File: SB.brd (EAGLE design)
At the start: 68 x 30 mm, 30 parts, among them IC1 ATMEGA32U4NT-TQFP, J1 USB-6P-SMT, J3 AUDIO-JACK-PJ321, J4 NO/NC, J5 RJ10-WURTH, K1 HE721C-DIP, Q1 2N7002

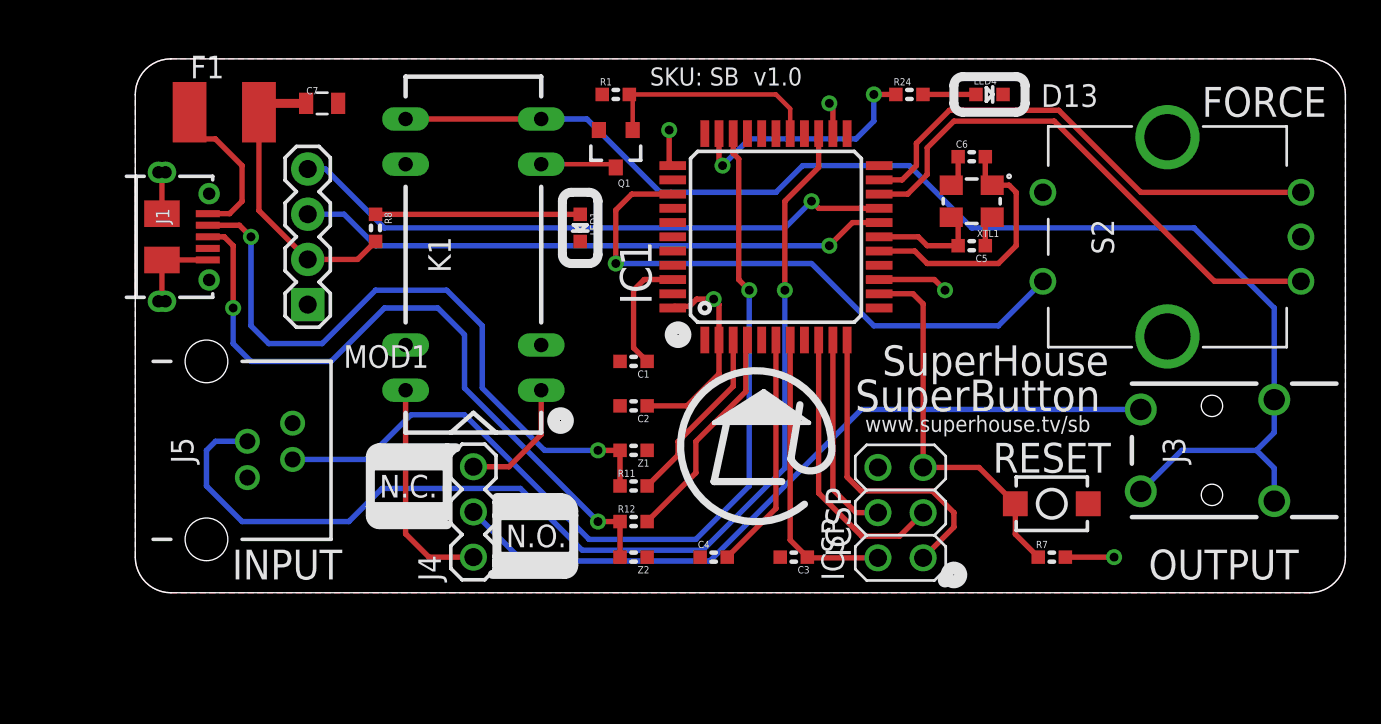
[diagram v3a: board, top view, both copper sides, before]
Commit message: Replaced RJ10 socket with RJ12 and added haptic feedback output
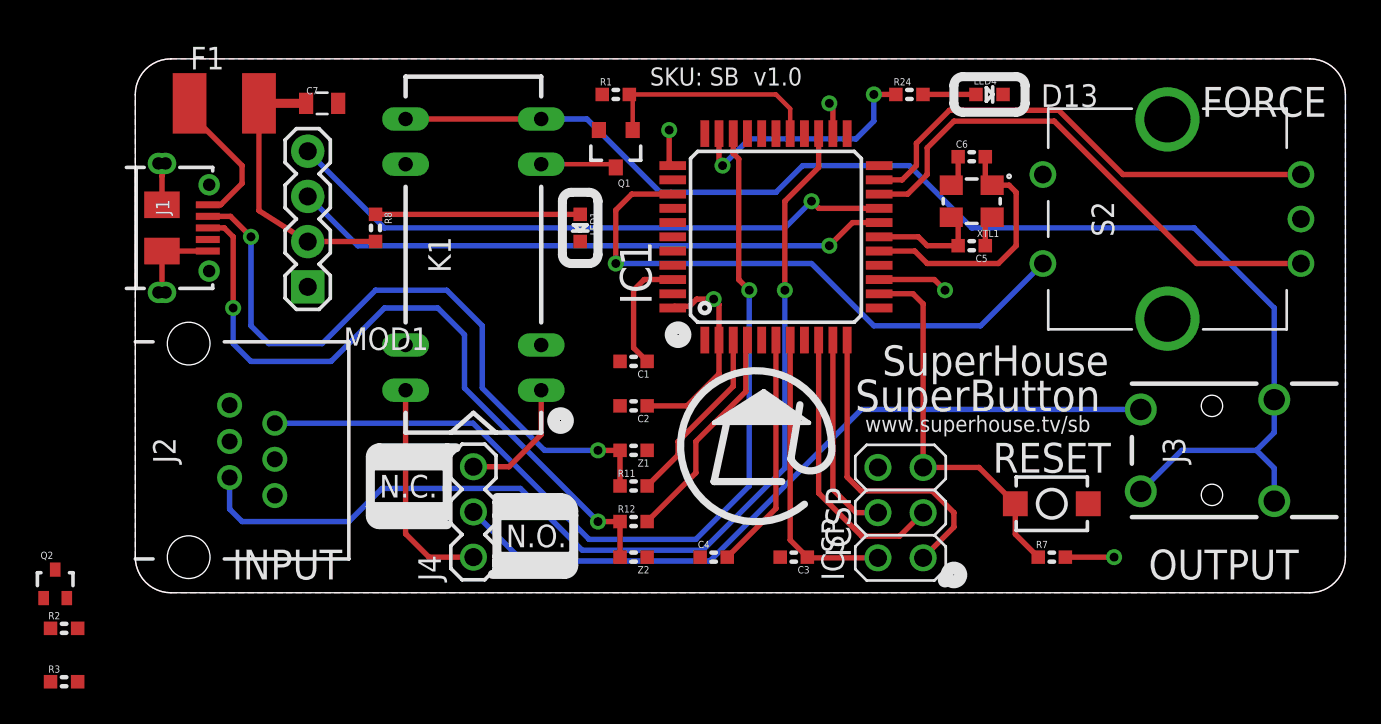
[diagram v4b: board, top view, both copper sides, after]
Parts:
- removed J5: RJ10-WURTH, SuperHouse-Connectors:RJ10
- added J2: RJ12, SuperHouse-Connectors:RJ12
- added Q2: RJU003N03, SuperHouse-DiscreteSemi:SOT32-3
- added R2: 150R, SuperHouse-DiscreteSemi:R0603
- added R3: 10K, SuperHouse-DiscreteSemi:R0603
- moved MOD1 1.00 mm to (28.0, 22.0)
- moved S2 1.00 mm to (58.0, 22.0)
- moved F1 0.50 mm to (5.00, 28.5)
- moved J1 0.50 mm to (1.50, 21.5)
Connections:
- new net N$2: J2.6, R2.2
- new net N$8: Q2.3, R2.1
- net 5V: now also J2.3, J2.4; no longer J5.P$1
- net D12: now also Q2.1, R3.2
- net D4_A6: now also J2.5; no longer J5.P$3
- net D5: now also J2.2; no longer J5.P$2
- net GND: now also J2.1, Q2.2, R3.1; no longer J5.P$4
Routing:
- net D4_A6: track 61.5 -> 57.0 mm
- net 5V: track 56.2 -> 55.2 mm
- net USB+: track 9.36 -> 8.70 mm
- net GND: track 10.9 -> 11.4 mm
- net D+: track 39.3 -> 39.8 mm

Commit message: Routing for haptic feedback
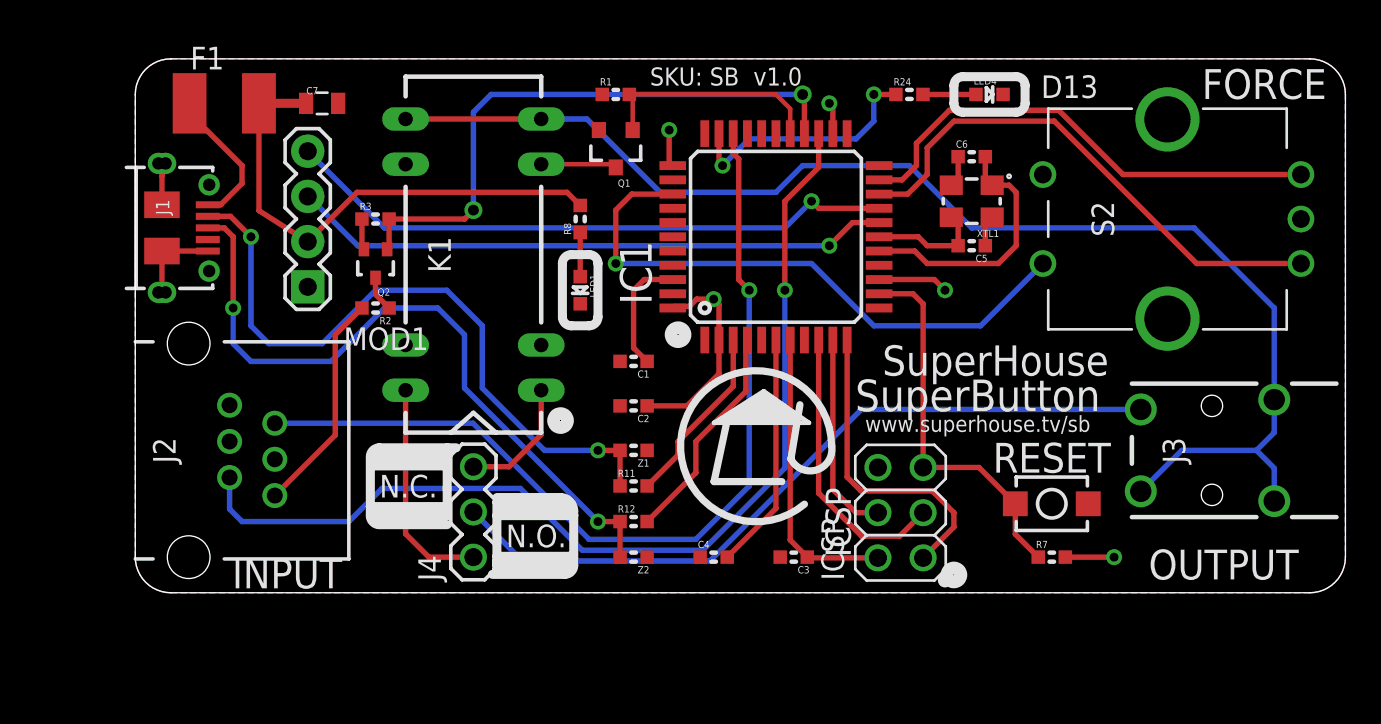
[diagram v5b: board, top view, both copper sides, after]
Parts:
- moved R3 31.3 mm to (13.5, 22.0)
- moved Q2 25.5 mm to (13.5, 19.5), turned to 180 degrees
- moved R2 25.1 mm to (13.5, 17.0), turned to 180 degrees
- moved R8 11.5 mm to (25.0, 22.0), turned to 90 degrees
- moved LED1 3.50 mm to (25.0, 18.0)
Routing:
- net D12: track 0.00 -> 33.3 mm, vias 0 -> 2
- net 5V: track 55.2 -> 68.1 mm
- net N$2: track 0.00 -> 12.6 mm
- net N$5: track 11.5 -> 2.48 mm
- net N$8: track 0.00 -> 2.02 mm
- net GND: track 11.4 -> 13.2 mm

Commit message: ERC / DRC for v1.0 release
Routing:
- net USB+: track 8.70 -> 8.14 mm
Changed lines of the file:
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@@
 <?xml version="1.0" encoding="utf-8"?>
 <!DOCTYPE eagle SYSTEM "eagle.dtd">
-<eagle version="9.5.2">
+<eagle version="9.5.1">
 <drawing>
 <settings>
@@
 <signal name="A0">
 <contactref element="IC1" pad="36"/>
-<wire x1="30.2" y1="23.4" x2="30.1072" y2="23.4928" width="0.3048" layer="1"/>
 <wire x1="30.2" y1="23.4" x2="27.9" y2="23.4" width="0.3048" layer="1"/>
 <wire x1="27.9" y1="23.4" x2="27" y2="22.5" width="0.3048" layer="1"/>
@@
 <contactref element="F1" pad="1"/>
 <wire x1="6" y1="24" x2="6" y2="25" width="0.3048" layer="1"/>
-<wire x1="3" y1="27.95" x2="3.05" y2="28.5" width="0.3048" layer="1"/>
 <wire x1="4.075" y1="22.8" x2="4.8" y2="22.8" width="0.3048" layer="1"/>
 <wire x1="4.8" y1="22.8" x2="6" y2="24" width="0.3048" layer="1"/>
@@
 <wire x1="14.262" y1="22" x2="18.5" y2="22" width="0.3048" layer="1"/>
 <wire x1="18.5" y1="22" x2="19" y2="22.5" width="0.3048" layer="1"/>
-<via x="19" y="22.5" extent="1-16" drill="0.6096"/>
+<via x="19" y="22.5" extent="1-16" drill="0.5"/>
 <wire x1="19" y1="22.5" x2="19" y2="28" width="0.3048" layer="16"/>
 <wire x1="20" y1="29" x2="37.5" y2="29" width="0.3048" layer="16"/>
-<via x="37.5" y="29" extent="1-16" drill="0.6096"/>
+<via x="37.5" y="29" extent="1-16" drill="0.5"/>
 <wire x1="37.5" y1="29" x2="37.6" y2="28.9" width="0.3048" layer="1"/>
 <wire x1="37.6" y1="28.9" x2="37.6" y2="26.8" width="0.3048" layer="1"/>

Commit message: Tweaks and cleanup, hopefully for v1.1 release
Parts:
- added R4: 10K, SuperHouse-DiscreteSemi:R0603
- Q2: value RJU003N03 -> 2N7002; device SuperHouse-DiscreteSemi:SOT32-3 -> SuperHouse-DiscreteSemi:SOT23-3
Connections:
- net 5V: now also R4.2
- net A0: now also R4.1
- net N$7: no longer J3.2
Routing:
- net N$7: track 73.6 -> 65.3 mm
- net 5V: track 68.1 -> 71.3 mm
- net A0: track 33.5 -> 36.5 mm
- net D2_SDA: track 34.7 -> 35.7 mm
- net D3_SCL: track 33.8 -> 34.6 mm
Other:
- board text added: "SKU: SB v1.1"
- board text removed: "SKU: SB v1.0"
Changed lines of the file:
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@@
 <?xml version="1.0" encoding="utf-8"?>
 <!DOCTYPE eagle SYSTEM "eagle.dtd">
-<eagle version="9.5.1">
+<eagle version="9.5.2">
 <drawing>
 <settings>
@@
 <setting verticaltext="up"/>
 </settings>
-<grid distance="0.5" unitdist="mm" unit="mm" style="lines" multiple="1" display="yes" altdistance="0.005" altunitdist="inch" altunit="inch"/>
+<grid distance="1" unitdist="mm" unit="mm" style="lines" multiple="1" display="yes" altdistance="0.005" altunitdist="inch" altunit="inch"/>
 <layers>
 <layer number="1" name="Top" color="12" fill="1" visible="yes" active="yes"/>
@@
 </layers>
 <board>
-<fusionsync huburn="a.cGVyc29uYWw6dWUyZDliZmNi" projecturn="a.cGVyc29uYWw6dWUyYmY2YTMwIzIwMTkxMjAzMjQ0MDMwNjUx" f3durn="urn:adsk.wipprod:dm.lineage:0njJKfu6R3STVv2jK1C-rg" pcbguid="d3339778-c5ae-47ed-addf-8a81f3fd190a" lastpulledtime="" lastsyncedchangeguid="e466276c-e581-ef05-ad4f-067f72518912"/>
+<fusionsync huburn="a.cGVyc29uYWw6dWUyZDliZmNi" projecturn="a.cGVyc29uYWw6dWUyYmY2YTMwIzIwMTkxMjAzMjQ0MDMwNjUx" f3durn="urn:adsk.wipprod:dm.lineage:0njJKfu6R3STVv2jK1C-rg" pcbguid="d3339778-c5ae-47ed-addf-8a81f3fd190a" lastpulledtime="" lastsyncedchangeguid="2cfb86e1-d0d8-e218-d1b3-489442767fc3"/>
 <plain>
 <wire x1="66" y1="31" x2="2" y2="31" width="0" layer="20"/>
@@
 <wire x1="68" y1="29" x2="66" y2="31" width="0" layer="20" curve="90"/>
 <text x="51.5" y="7.746" size="1.6764" layer="21" font="vector" ratio="15" align="bottom-center">RESET</text>
-<text x="28.92" y="29.5" size="1.016" layer="21" font="vector" ratio="18">SKU: SB  v1.0</text>
+<text x="28.92" y="29.5" size="1.016" layer="21" font="vector" ratio="18">SKU: SB  v1.1</text>
 <wire x1="39.126" y1="9.278" x2="37.602" y2="5.976" width="0.4064" layer="21" curve="309.2564"/>
 <wire x1="39.126" y1="9.278" x2="36.84" y2="8.516" width="0.4064" layer="21" curve="-163.361194"/>
@@
 <text x="47.34" y="10.04" size="0.9" layer="21" font="vector" ratio="18" align="bottom-center">www.superhouse.tv/sb</text>
 <text x="48.34" y="13.2" size="1.7" layer="21" font="vector" ratio="18" align="bottom-center">SuperHouse</text>
+<wire x1="20.75" y1="5.75" x2="24" y2="5.75" width="1.016" layer="21"/>
+<wire x1="20.75" y1="2.5" x2="24" y2="2.5" width="1.016" layer="21"/>
+<wire x1="17" y1="5.25" x2="14" y2="5.25" width="1.016" layer="21"/>
+<wire x1="13.75" y1="8.5" x2="17" y2="8.5" width="1.016" layer="21"/>
 </plain>
 <attributes>
@@
 <attribute name="VALUE" x="-1" y="9" size="1.27" layer="27" rot="R270" align="bottom-center"/>
 </element>
-<element name="Q2" library="SuperHouse-DiscreteSemi" library_urn="urn:adsk.eagle:library:11768461" package="SOT32-3" package3d_urn="urn:adsk.eagle:package:7066313/2" value="RJU003N03" x="13.5" y="19.5" smashed="yes" rot="R180">
+<element name="Q2" library="SuperHouse-DiscreteSemi" library_urn="urn:adsk.eagle:library:11768461" package="SOT23-3" package3d_urn="urn:adsk.eagle:package:11815952/3" value="2N7002" x="13.5" y="19.5" smashed="yes" rot="R180">
 <attribute name="NAME" x="14.3255" y="18.1" size="0.4064" layer="25" rot="R180"/>
 <attribute name="VALUE" x="14.3" y="19.6905" size="0.3048" layer="27" rot="R180"/>
@@
 <attribute name="NAME" x="12.611" y="22.508" size="0.4064" layer="25" font="vector"/>
 <attribute name="VALUE" x="12.484" y="21.0348" size="0.4064" layer="27" font="vector"/>
+</element>
+<element name="R4" library="SuperHouse-DiscreteSemi" library_urn="urn:adsk.eagle:library:11768461" package="R0603" package3d_urn="urn:adsk.eagle:package:11768543/2" value="10K" x="49" y="17" smashed="yes" rot="R180">
+<attribute name="NAME" x="49.889" y="16.492" size="0.4064" layer="25" font="vector" rot="R180"/>
+<attribute name="VALUE" x="50.016" y="17.9652" size="0.4064" layer="27" font="vector" rot="R180"/>
 </element>
 </elements>
@@
 <wire x1="38" y1="19.5" x2="41.5" y2="16" width="0.3048" layer="16"/>
 <wire x1="41.5" y1="16" x2="47.5" y2="16" width="0.3048" layer="16"/>
+<contactref element="R4" pad="1"/>
+<wire x1="49.762" y1="17" x2="51" y2="18.238" width="0.3048" layer="1"/>
+<wire x1="51" y1="18.238" x2="51" y2="19.5" width="0.3048" layer="1"/>
 </signal>
 <signal name="A1">
@@
 <wire x1="9.69" y1="20.73" x2="12.46" y2="23.5" width="0.3048" layer="1"/>
 <wire x1="12.46" y1="23.5" x2="24.262" y2="23.5" width="0.3048" layer="1"/>
+<contactref element="R4" pad="2"/>
+<wire x1="48.238" y1="17" x2="47.238" y2="18" width="0.3048" layer="1"/>
+<wire x1="47.238" y1="18" x2="45.5" y2="18" width="0.3048" layer="1"/>
 </signal>
 <signal name="RESET">
@@
 <contactref element="R3" pad="1"/>
 <wire x1="12.738" y1="22" x2="12.738" y2="20.412" width="0.3048" layer="1"/>
-<wire x1="12.738" y1="20.412" x2="12.85" y2="20.3" width="0.3048" layer="1"/>
+<wire x1="12.738" y1="20.412" x2="12.55" y2="20.5" width="0.3048" layer="1"/>
 </signal>
 <signal name="3V3">
@@
 <contactref element="R3" pad="2"/>
 <wire x1="14.262" y1="22" x2="14.262" y2="20.412" width="0.3048" layer="1"/>
-<wire x1="14.262" y1="20.412" x2="14.15" y2="20.3" width="0.3048" layer="1"/>
-<wire x1="14.262" y1="22" x2="18.5" y2="22" width="0.3048" layer="1"/>
-<wire x1="18.5" y1="22" x2="19" y2="22.5" width="0.3048" layer="1"/>
-<via x="19" y="22.5" extent="1-16" drill="0.5"/>
-<wire x1="19" y1="22.5" x2="19" y2="28" width="0.3048" layer="16"/>
+<wire x1="14.262" y1="20.412" x2="14.45" y2="20.5" width="0.3048" layer="1"/>
+<wire x1="14.262" y1="22" x2="19" y2="22" width="0.3048" layer="1"/>
+<via x="19" y="22" extent="1-16" drill="0.5"/>
+<wire x1="19" y1="22" x2="19" y2="28" width="0.3048" layer="16"/>
 <wire x1="20" y1="29" x2="37.5" y2="29" width="0.3048" layer="16"/>
 <via x="37.5" y="29" extent="1-16" drill="0.5"/>
@@
 <signal name="D4_A6">
 <contactref element="IC1" pad="25"/>
-<wire x1="38.4" y1="26.8" x2="38.4" y2="24.9" width="0.3048" layer="1"/>
-<wire x1="36.5" y1="23" x2="36.5" y2="18" width="0.3048" layer="1"/>
+<wire x1="38.4" y1="26.8" x2="38.4" y2="25.65" width="0.3048" layer="1"/>
+<wire x1="36.5" y1="23.75" x2="36.5" y2="18" width="0.3048" layer="1"/>
 <via x="36.5" y="18" extent="1-16" drill="0.5"/>
-<wire x1="38.4" y1="24.9" x2="36.5" y2="23" width="0.3048" layer="1"/>
+<wire x1="38.4" y1="25.65" x2="36.5" y2="23.75" width="0.3048" layer="1"/>
 <wire x1="36.5" y1="18" x2="36.5" y2="8" width="0.3048" layer="16"/>
 <wire x1="31.8904" y1="3.3904" x2="25.1096" y2="3.3904" width="0.3048" layer="16"/>
@@
 <contactref element="IC1" pad="19"/>
 <contactref element="MOD1" pad="SDA"/>
-<wire x1="36.5" y1="21.5" x2="14" y2="21.5" width="0.3048" layer="16"/>
-<wire x1="36.5" y1="21.5" x2="38" y2="23" width="0.3048" layer="16"/>
-<via x="38" y="23" extent="1-16" drill="0.5"/>
-<wire x1="38" y1="23" x2="38.4" y2="22.6" width="0.3048" layer="1"/>
-<wire x1="38.4" y1="22.6" x2="41.8" y2="22.6" width="0.3048" layer="1"/>
-<wire x1="14" y1="21.5" x2="9.69" y2="25.81" width="0.3048" layer="16"/>
+<wire x1="37" y1="21.5" x2="22.5" y2="21.5" width="0.3048" layer="16"/>
+<wire x1="22.5" y1="21.5" x2="21.25" y2="20.25" width="0.3048" layer="16"/>
+<wire x1="21.25" y1="20.25" x2="15.25" y2="20.25" width="0.3048" layer="16"/>
+<wire x1="37" y1="21.5" x2="38.5" y2="23" width="0.3048" layer="16"/>
+<via x="38.5" y="23" extent="1-16" drill="0.5"/>
+<wire x1="38.9" y1="22.6" x2="38.5" y2="23" width="0.3048" layer="1"/>
+<wire x1="38.9" y1="22.6" x2="41.8" y2="22.6" width="0.3048" layer="1"/>
+<wire x1="15.25" y1="20.25" x2="9.69" y2="25.81" width="0.3048" layer="16"/>
 </signal>
 <signal name="D3_SCL">
 <contactref element="IC1" pad="18"/>
 <contactref element="MOD1" pad="SCL"/>
-<wire x1="12.5" y1="20.5" x2="39" y2="20.5" width="0.3048" layer="16"/>
+<wire x1="13.5" y1="19.5" x2="21.5" y2="19.5" width="0.3048" layer="16"/>
+<wire x1="21.5" y1="19.5" x2="22.5" y2="20.5" width="0.3048" layer="16"/>
+<wire x1="22.5" y1="20.5" x2="39" y2="20.5" width="0.3048" layer="16"/>
 <via x="39" y="20.5" extent="1-16" drill="0.5"/>
 <wire x1="39" y1="20.5" x2="40.3" y2="21.8" width="0.3048" layer="1"/>
 <wire x1="40.3" y1="21.8" x2="41.8" y2="21.8" width="0.3048" layer="1"/>
 <wire x1="9.73" y1="23.27" x2="9.69" y2="23.27" width="0.3048" layer="16"/>
-<wire x1="12.5" y1="20.5" x2="9.73" y2="23.27" width="0.3048" layer="16"/>
+<wire x1="13.5" y1="19.5" x2="9.73" y2="23.27" width="0.3048" layer="16"/>
 </signal>
 <signal name="N$1">
@@
 </signal>
 <signal name="N$7">
-<contactref element="J3" pad="2"/>
 <contactref element="J3" pad="4B"/>
 <contactref element="J3" pad="4A"/>
 <contactref element="K1" pad="7"/>
 <contactref element="K1" pad="8"/>
-<wire x1="56.5" y1="6.7" x2="58.8" y2="9" width="0.3048" layer="16"/>
-<wire x1="58.8" y1="9" x2="63" y2="9" width="0.3048" layer="16"/>
-<wire x1="63" y1="9" x2="64" y2="8" width="0.3048" layer="16"/>
-<wire x1="64" y1="8" x2="64" y2="6.15" width="0.3048" layer="16"/>
-<wire x1="64" y1="11.85" x2="64" y2="10" width="0.3048" layer="16"/>
-<wire x1="64" y1="10" x2="63" y2="9" width="0.3048" layer="16"/>
 <wire x1="22.81" y1="27.62" x2="25.38" y2="27.62" width="0.3048" layer="16"/>
 <wire x1="36" y1="23.5" x2="37.5" y2="25" width="0.3048" layer="16"/>
@@
 <wire x1="47" y1="21.5" x2="59.5" y2="21.5" width="0.3048" layer="16"/>
 <wire x1="15.19" y1="27.62" x2="22.81" y2="27.62" width="0.3048" layer="1"/>
+<wire x1="64" y1="11.85" x2="64" y2="6.15" width="0.3048" layer="16"/>
 </signal>
 <signal name="N$2">
@@
 <contactref element="R2" pad="1"/>
 <contactref element="Q2" pad="3"/>
-<wire x1="13.5" y1="18.7" x2="13.5" y2="17.762" width="0.3048" layer="1"/>
+<wire x1="13.5" y1="18.4" x2="13.5" y2="17.762" width="0.3048" layer="1"/>
 <wire x1="13.5" y1="17.762" x2="14.262" y2="17" width="0.3048" layer="1"/>
 </signal>
